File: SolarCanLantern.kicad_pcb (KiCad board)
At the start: 2 copper layers, 14 parts, among them Q1 2N7002, Q2 2N7002, Q3 2N7002, Q4 2N7002, U1 ATTINY13-20SSU

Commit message: start of layout
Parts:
- added BT1: Battery_Cell, Socket_Strips:Socket_Strip_Straight_1x02_Pitch2.54mm, F.Cu at (154.0, 106.0)
- added SC1: Solar_Cell, Socket_Strips:Socket_Strip_Straight_1x02_Pitch2.54mm, F.Cu at (134.0, 106.0)
- R1: value R -> 287K
- R2: value R -> 88.7K
- moved D3 45.5 mm to (144.0, 137.0)
- moved D4 45.5 mm to (144.0, 106.0), turned to 180 degrees
- moved Q4 37.8 mm to (135.0, 115.0), turned to 180 degrees
- moved Q3 33.6 mm to (135.0, 138.0), turned to 90 degrees
- moved R5 33.4 mm to (152.0, 137.0), turned to 180 degrees
- moved R2 27.1 mm to (156.0, 119.0), turned to 270 degrees
- moved R1 22.8 mm to (156.0, 113.0), turned to 270 degrees
- moved D2 15.8 mm to (170.0, 112.0)
- moved U1 15.8 mm to (147.0, 118.0)
- moved Q2 11.4 mm to (161.0, 113.0), turned to 90 degrees
- moved R4 10.4 mm to (178.0, 112.0), turned to 180 degrees
- moved D1 9.04 mm to (170.0, 118.0)
- moved R3 6.68 mm to (178.0, 118.0), turned to 180 degrees
- moved Q1 4.91 mm to (161.0, 119.0), turned to 90 degrees
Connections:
- Q3 pad 1: /LEDC -> (no net)
- U1 pad 1: Net-(U1-Pad1) -> (no net)
- U1 pad 2: /VBatt_Divider -> /~SOLAR
- U1 pad 3: /Switch -> (no net)
- U1 pad 7: /~SOLAR -> /VBatt_Divider

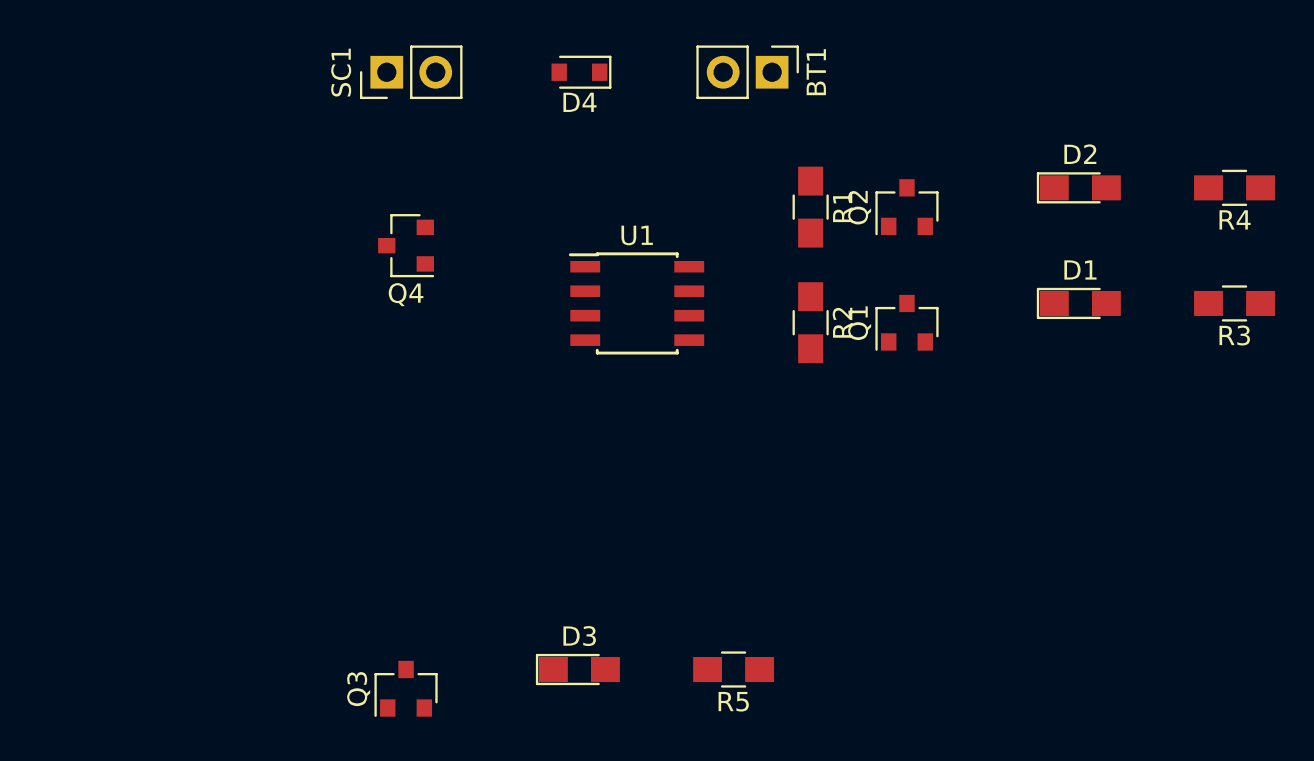
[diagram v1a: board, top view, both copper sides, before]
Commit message: first rev pcb layout with no button
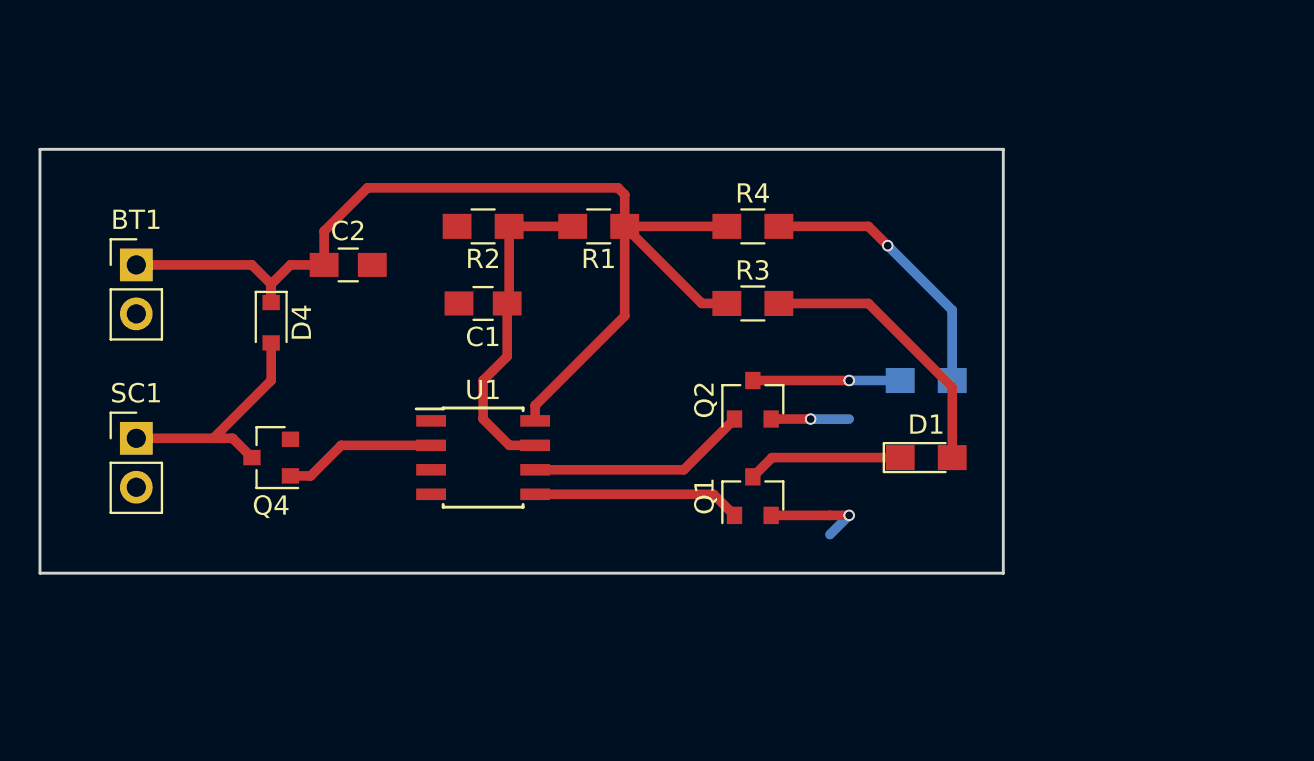
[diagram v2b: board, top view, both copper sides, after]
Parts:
- removed D3: LED, LEDs:LED_0805_HandSoldering
- removed Q3: 2N7002, TO_SOT_Packages_SMD:SOT-23
- removed R5: 10Ω, Resistors_SMD:R_0805_HandSoldering
- added C1: 0.1µF, Capacitors_SMD:C_0805_HandSoldering, F.Cu at (139.0, 118.0)
- added C2: 10µF, Capacitors_SMD:C_0805_HandSoldering, F.Cu at (132.0, 116.0)
- D2: moved to B.Cu
- moved BT1 34.5 mm to (121.0, 116.0), turned to 0 degrees
- moved R4 25.1 mm to (153.0, 114.0), turned to 0 degrees
- moved R3 25.0 mm to (153.0, 118.0), turned to 0 degrees
- moved SC1 23.0 mm to (121.0, 125.0), turned to 0 degrees
- moved D4 20.6 mm to (128.0, 119.0), turned to 270 degrees
- moved R2 17.7 mm to (139.0, 114.0), turned to 180 degrees
- moved Q4 13.0 mm to (128.0, 126.0)
- moved D2 12.8 mm to (162.0, 122.0)
- moved Q2 12.8 mm to (153.0, 123.0)
- moved Q1 12.0 mm to (153.0, 128.0)
- moved D1 11.3 mm to (162.0, 126.0)
- moved U1 11.3 mm to (139.0, 126.0)
- moved R1 11.0 mm to (145.0, 114.0), turned to 180 degrees
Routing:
- net +BATT: track 0.00 -> 56.9 mm
- net /VBatt_Divider: track 0.00 -> 17.1 mm
- net Net-(D2-Pad2): track 0.00 -> 14.5 mm, vias 0 -> 1
- net Net-(D1-Pad2): track 0.00 -> 14.5 mm
- net Net-(D4-Pad2): track 0.00 -> 12.6 mm
- net /LEDB: track 0.00 -> 11.4 mm
- net /LEDA: track 0.00 -> 10.8 mm
- net GND: track 0.00 -> 9.51 mm, vias 0 -> 2
- net Net-(D1-Pad1): track 0.00 -> 8.06 mm
- net /~SOLAR: track 0.00 -> 7.96 mm
- net Net-(D2-Pad1): track 0.00 -> 7.65 mm, vias 0 -> 1
- added copper zone on B.Cu, net GND
- added copper zone on F.Cu, net GND
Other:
- board outline added: 50 x 22 mm
- net class Default: trace_width 0.25 -> 0.5

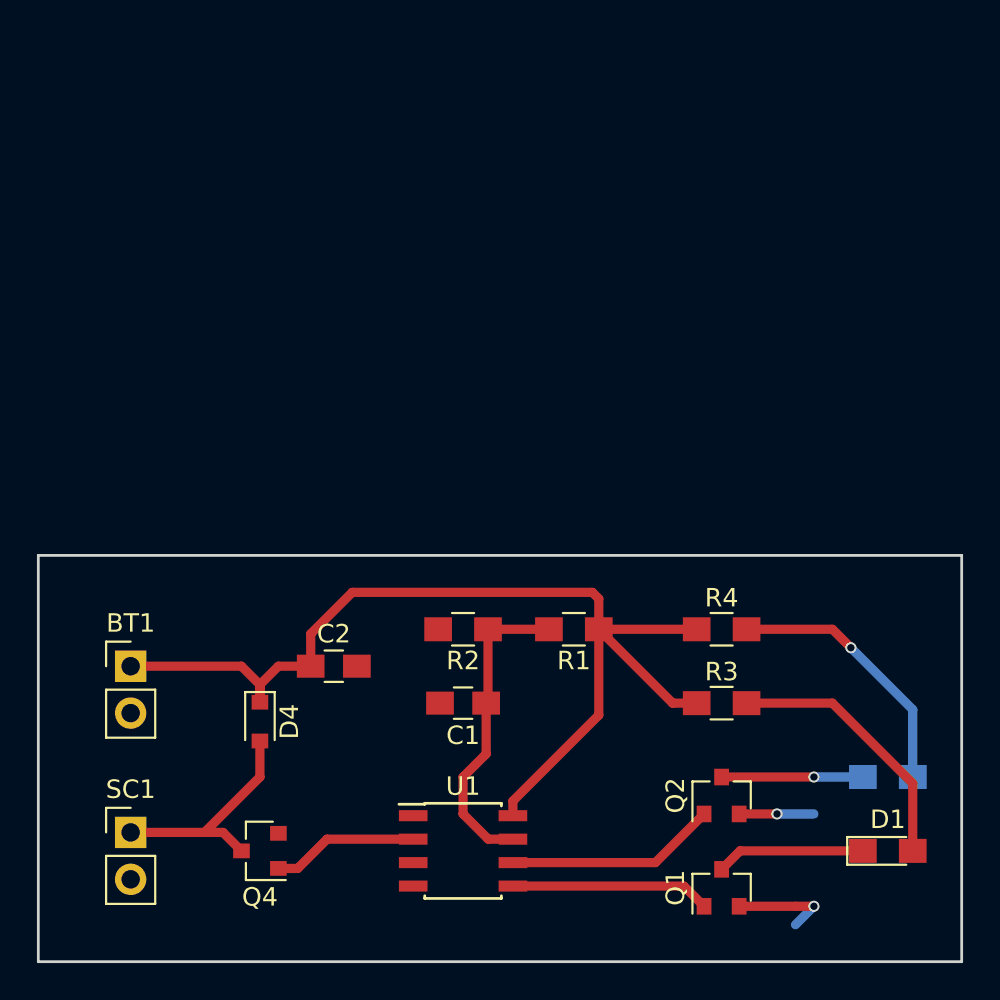
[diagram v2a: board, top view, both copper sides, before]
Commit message: Added switch and completed first PCB layout
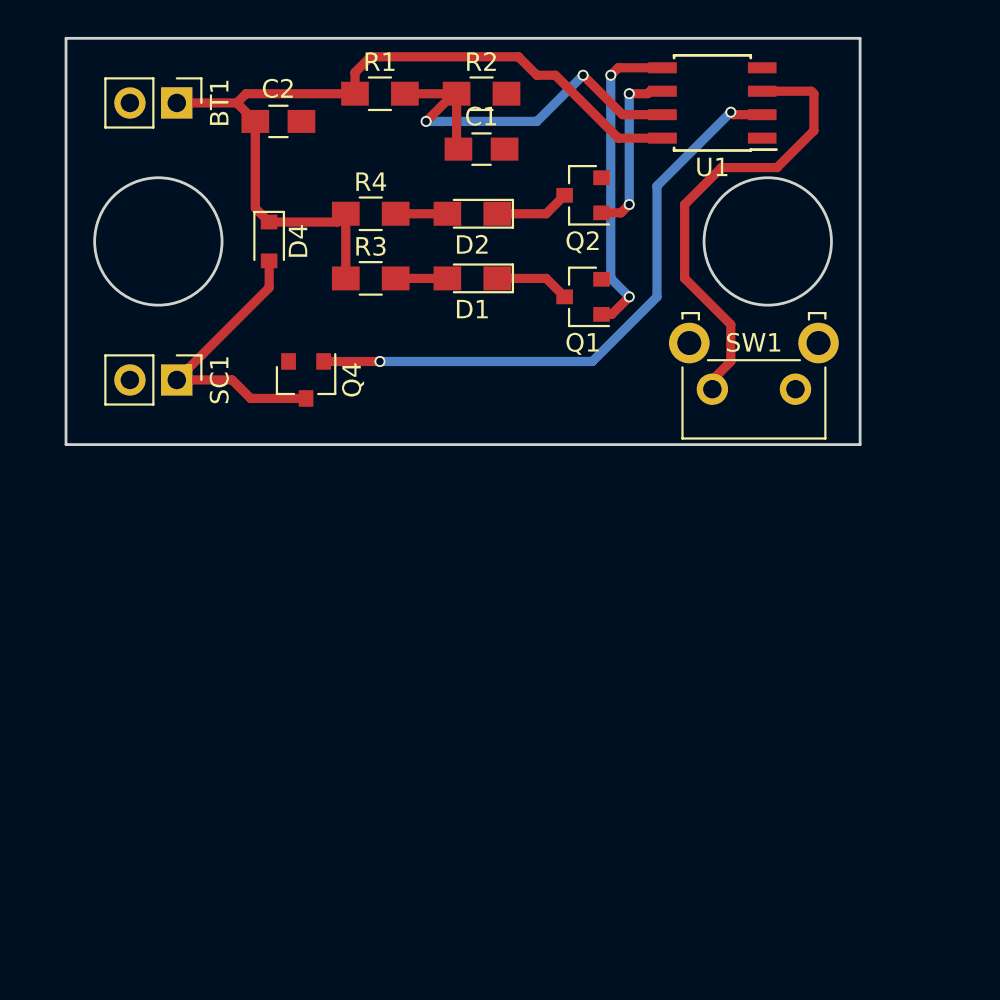
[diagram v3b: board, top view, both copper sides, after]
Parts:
- added SW1: SW_Push, Buttons_Switches_THT:SW_Tactile_SKHH_Angled, F.Cu at (157.0, 101.0)
- D2: moved to F.Cu
- moved U1 42.7 mm to (152.5, 85.5), turned to 180 degrees
- moved D1 38.3 mm to (139.5, 95.0), turned to 180 degrees
- moved D2 37.9 mm to (139.5, 91.5), turned to 180 degrees
- moved Q2 33.4 mm to (145.5, 90.5), turned to 180 degrees
- moved Q1 32.9 mm to (145.5, 96.0), turned to 180 degrees
- moved R1 30.8 mm to (134.5, 85.0), turned to 0 degrees
- moved BT1 30.6 mm to (123.5, 85.5), turned to 270 degrees
- moved C1 30.0 mm to (140.0, 88.0), turned to 0 degrees
- moved R3 29.8 mm to (134.0, 95.0)
- moved C2 29.7 mm to (129.0, 86.5)
- moved R4 29.4 mm to (134.0, 91.5)
- moved R2 29.0 mm to (140.0, 85.0), turned to 0 degrees
- moved D4 26.0 mm to (128.5, 93.0)
- moved Q4 25.6 mm to (130.5, 100.5), turned to 270 degrees
- moved SC1 24.6 mm to (123.5, 100.5), turned to 270 degrees
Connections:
- U1 pad 3: (no net) -> /Switch
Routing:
- net /Switch: track 0.00 -> 25.0 mm
- net /~SOLAR: track 7.96 -> 32.9 mm, vias 0 -> 2
- net +BATT: track 56.9 -> 44.8 mm
- net Net-(D2-Pad2): track 14.5 -> 2.80 mm, vias 1 -> 0
- net Net-(D1-Pad2): track 14.5 -> 2.80 mm
- net GND: track 9.51 -> 0.00 mm, vias 2 -> 0
- net /LEDA: track 10.8 -> 17.3 mm, vias 0 -> 2
- net /VBatt_Divider: track 17.1 -> 22.8 mm, vias 0 -> 2
- net Net-(D1-Pad1): track 8.06 -> 4.06 mm
- net Net-(D2-Pad1): track 7.65 -> 4.06 mm, vias 1 -> 0
- net Net-(D4-Pad2): track 12.6 -> 15.9 mm
- net /LEDB: track 11.4 -> 9.54 mm, vias 0 -> 2
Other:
- board size 50 x 22 mm -> 43 x 22 mm
- board text added: "HMC Haiti Solar Lights Project 2018 PCB Rev. 2"

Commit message: got latest version from tejus and modified
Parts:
- removed D4: D, Diodes_SMD:D_0805
- removed Q4: 2N7002, TO_SOT_Packages_SMD:SOT-23
- added U2: MAX40200, TO_SOT_Packages_SMD:TSOT-23-5_HandSoldering, F.Cu at (202.4, 86.4)
- D2: moved to B.Cu
- moved R3 91.1 mm to (224.3, 82.5), turned to 270 degrees
- moved R4 87.7 mm to (221.2, 82.5), turned to 270 degrees
- moved D1 86.3 mm to (225.5, 88.3), turned to 90 degrees
- moved D2 86.1 mm to (225.5, 88.3), turned to 90 degrees
- moved C2 84.1 mm to (213.1, 88.4), turned to 180 degrees
- moved BT1 83.7 mm to (207.0, 80.3), turned to 90 degrees
- moved SC1 78.8 mm to (199.6, 80.3), turned to 90 degrees
- moved R2 77.7 mm to (217.7, 83.6), turned to 90 degrees
- moved R1 75.6 mm to (210.1, 85.3)
- moved C1 75.3 mm to (215.1, 83.5), turned to 90 degrees
- moved Q1 75.3 mm to (220.7, 94.0), turned to 0 degrees
- moved Q2 75.2 mm to (220.7, 89.4), turned to 0 degrees
- moved U1 61.3 mm to (213.4, 92.5), turned to 0 degrees
- moved SW1 48.3 mm to (204.9, 95.2)
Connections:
- SC1 pad 1: Net-(D4-Pad2) -> /SolarIn
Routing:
- net /~SOLAR: track 32.9 -> 13.2 mm, vias 2 -> 0
- net Net-(D4-Pad2): track 15.9 -> 0.00 mm
- net GND: track 0.00 -> 14.0 mm, vias 0 -> 4
- net /LEDA: track 17.3 -> 4.23 mm, vias 2 -> 0
- net /Switch: track 25.0 -> 12.1 mm
- net +BATT: track 44.8 -> 34.7 mm
- net /SolarIn: track 0.00 -> 5.60 mm
- net /VBatt_Divider: track 22.8 -> 18.3 mm
- net Net-(D2-Pad2): track 2.80 -> 6.17 mm, vias 0 -> 1
- net /LEDB: track 9.54 -> 6.47 mm, vias 2 -> 0
- net Net-(D1-Pad1): track 4.06 -> 5.88 mm
- net Net-(D1-Pad2): track 2.80 -> 4.22 mm
- net Net-(D2-Pad1): track 4.06 -> 3.87 mm, vias 0 -> 1
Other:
- board size 43 x 22 mm -> 30.5 x 19 mm
- net class Default: clearance 0.2 -> 0.25; trace_width 0.5 -> 0.3
- rule pad_to_mask_clearance: 0.2 -> 0
- rule trace_clearance: 0.2 -> 0.25
- board text added: "Haiti Solar Lights Project Tejus Rao and Erik Meike 2018"
- board text removed: "HMC Haiti Solar Lights Project 2018 PCB Rev. 2"
